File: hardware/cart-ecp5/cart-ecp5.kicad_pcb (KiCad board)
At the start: 4 copper layers, 100 x 60 mm, 136 parts, among them J1 JTAG, J2 MicroSD_Molex_1040310811, J3 N64_Cartridge_Bus, J5 USB_C_USB2.0, U1 LFE5U-25F-xBG256x, U10 93C46BT-I_OT, U11 FT2232HQ, U12 TPS2121, U13 TLV62568DBV, U2 W25Q128JVSIM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

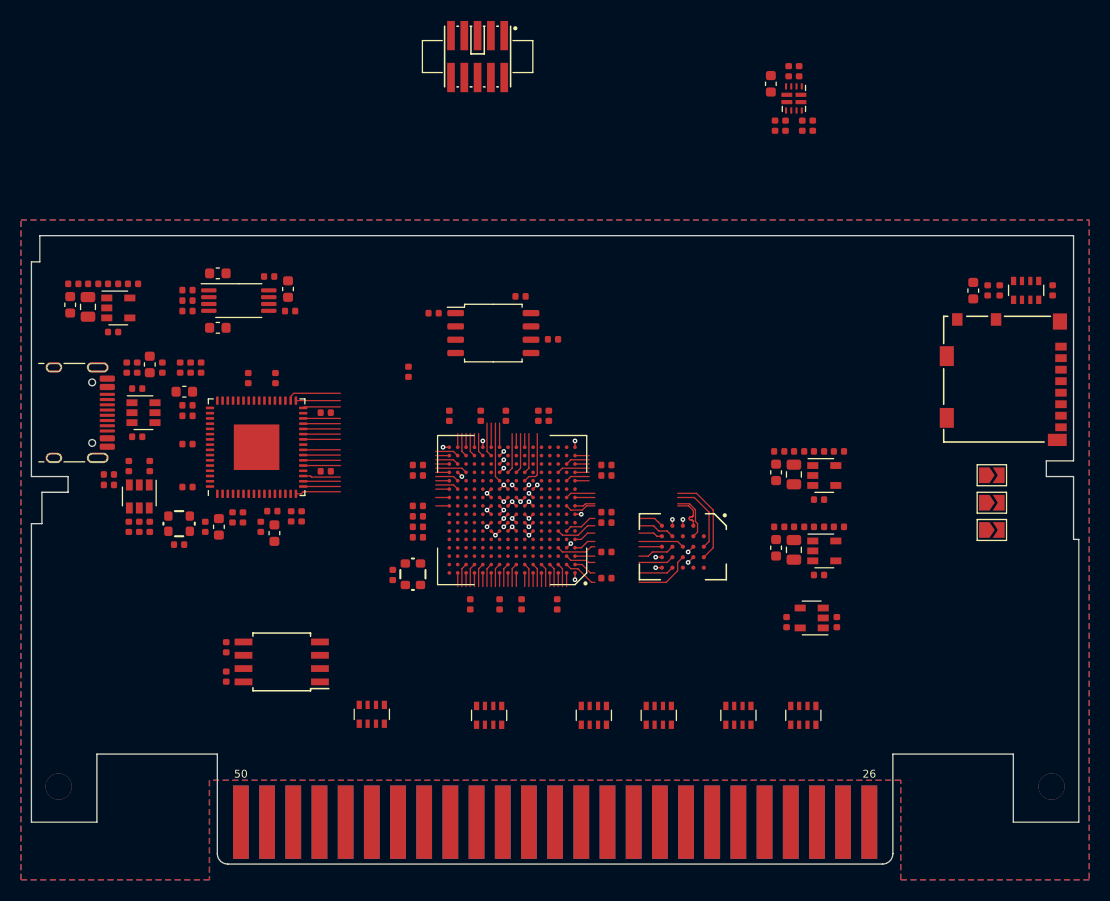
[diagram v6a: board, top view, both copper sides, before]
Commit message: Update config flash to WSON package, add HyperRAM decoupling
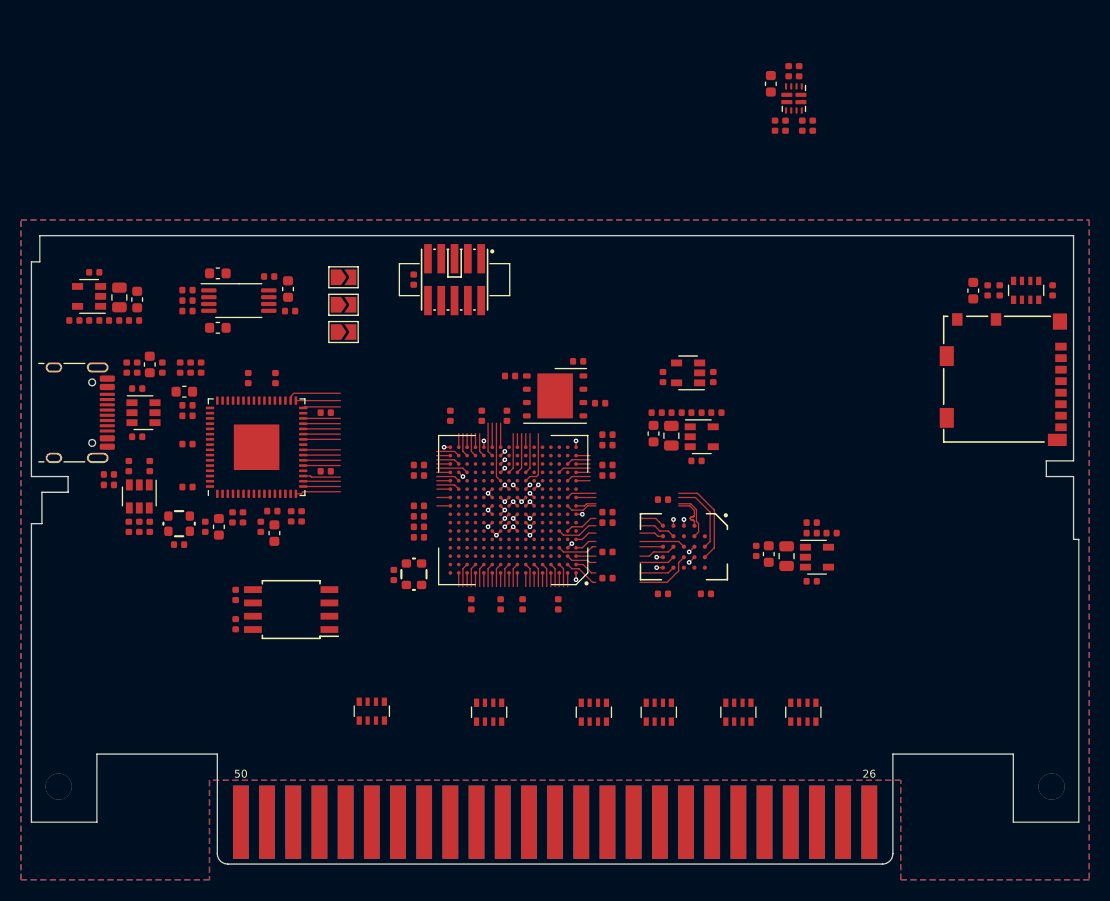
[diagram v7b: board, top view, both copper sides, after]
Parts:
- added C69: 100n, Capacitor_SMD:C_0402_1005Metric, F.Cu at (160.3, 108.2)
- added C70: 100n, Capacitor_SMD:C_0402_1005Metric, F.Cu at (164.4, 108.2)
- added C71: 100n, Capacitor_SMD:C_0402_1005Metric, F.Cu at (160.3, 99.2)
- U2: value W25Q128JVSIM -> W25Q512JVEIM; footprint Package_SO:SOIC-8_5.275x5.275mm_P1.27mm -> Package_SON:WSON-8-1EP_6x5mm_P1.27mm_EP3.4x4.3mm
- moved JP1 64.7 mm to (129.8, 80.6)
- moved JP2 64.7 mm to (129.8, 78.0)
- moved JP3 64.7 mm to (129.8, 83.2)
- moved C12 26.2 mm to (165.1, 87.5)
- moved U8 26.2 mm to (162.7, 87.1)
- moved C13 26.2 mm to (160.3, 87.5)
- moved J1 21.4 mm to (140.4, 78.2)
- moved L2 12.3 mm to (161.1, 93.1)
- moved C15 12.3 mm to (161.6, 90.9)
- moved C19 12.3 mm to (159.7, 90.9)
- moved C11 12.3 mm to (163.5, 95.5)
- moved U7 12.3 mm to (164.0, 93.2)
- moved C17 12.3 mm to (159.4, 92.9)
- moved R12 12.3 mm to (163.5, 90.9)
- moved R13 12.3 mm to (165.4, 90.9)
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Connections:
- U2 pad 4: GND -> Net-(U2-Pad4)
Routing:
- added copper zone on In2.Cu(PWR), net P1V1
- added copper zone on In2.Cu(PWR), net P1V8

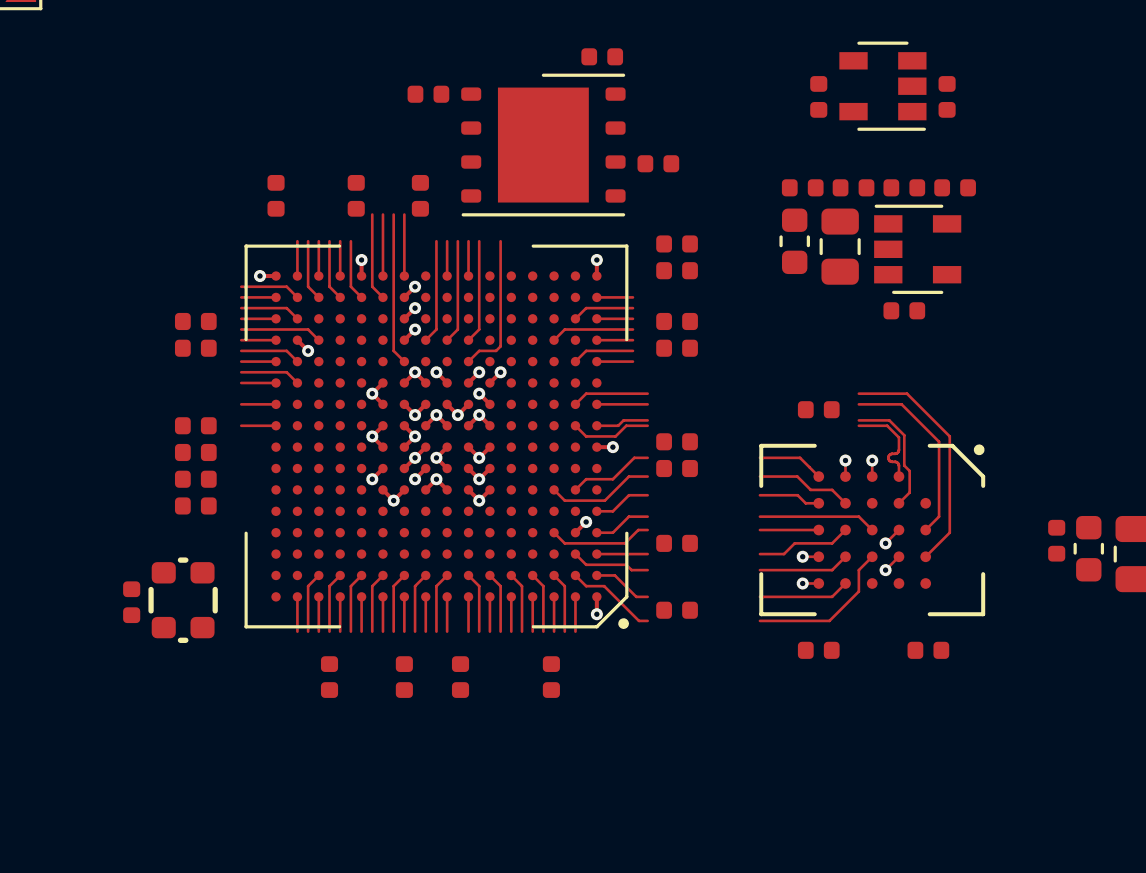
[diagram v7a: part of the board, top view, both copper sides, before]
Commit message: Preliminary core and HyperRAM power design
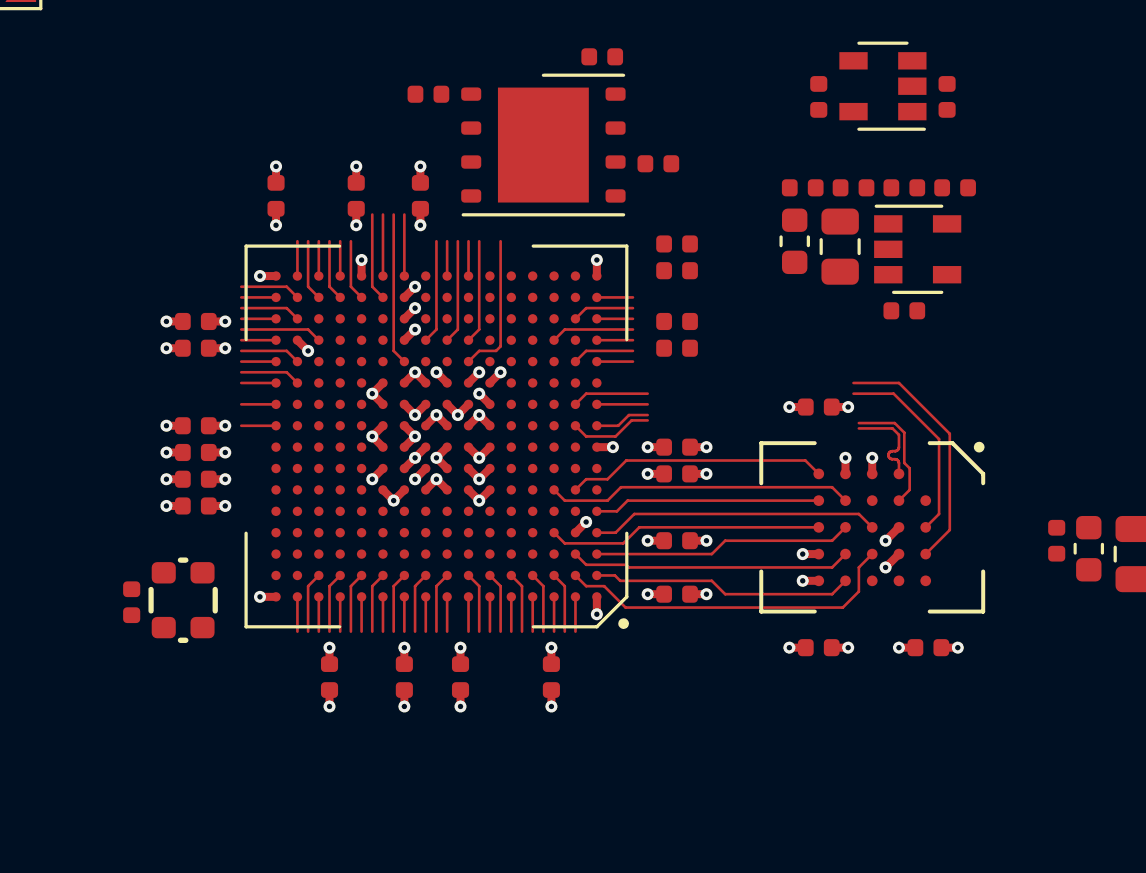
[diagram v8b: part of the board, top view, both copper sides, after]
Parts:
- moved C62 0.60 mm to (155.0, 106.1)
- moved C42 0.20 mm to (155.0, 101.6)
- moved C43 0.20 mm to (155.0, 100.6)
- moved C55 0.10 mm to (155.0, 104.1)
- moved C69 0.10 mm to (160.3, 108.1)
- moved C70 0.10 mm to (164.4, 108.1)
- moved C71 0.10 mm to (160.3, 99.1)
- moved U3 0.10 mm to (162.3, 103.6)
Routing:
- net GND: track 15.7 -> 28.6 mm, vias 20 -> 41
- net P3V3: track 6.79 -> 11.7 mm, vias 7 -> 15
- net HRAM_DQ0: track 5.47 -> 9.71 mm
- net HRAM_DQ5: track 6.07 -> 10.3 mm
- net HRAM_RWDS: track 6.56 -> 10.8 mm
- net HRAM_DQ3: track 6.36 -> 10.5 mm
- net HRAM_DQ4: track 5.64 -> 9.80 mm
- net HRAM_DQ7: track 5.69 -> 9.76 mm
- net HRAM_DQ6: track 4.47 -> 8.47 mm
- net HRAM_DQ2: track 9.07 -> 13.0 mm
- net HRAM_DQ1: track 7.65 -> 11.5 mm
- net P1V1: track 3.39 -> 7.08 mm, vias 4 -> 10
- net P1V8: track 3.04 -> 6.11 mm, vias 4 -> 9
- net P2V5: track 1.13 -> 1.75 mm, vias 2 -> 3
